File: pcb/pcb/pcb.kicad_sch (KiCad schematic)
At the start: 27 parts, among them J1 Conn_01x28_Socket, J2 Conn_01x28_Socket, J3 Conn_01x03_Socket, J4 Conn_01x04_Socket, J5 MAX17048, J6 LSM6DS3TR-C, J7 SSD1306, SW1 SW_SPST, U1 TPS61022

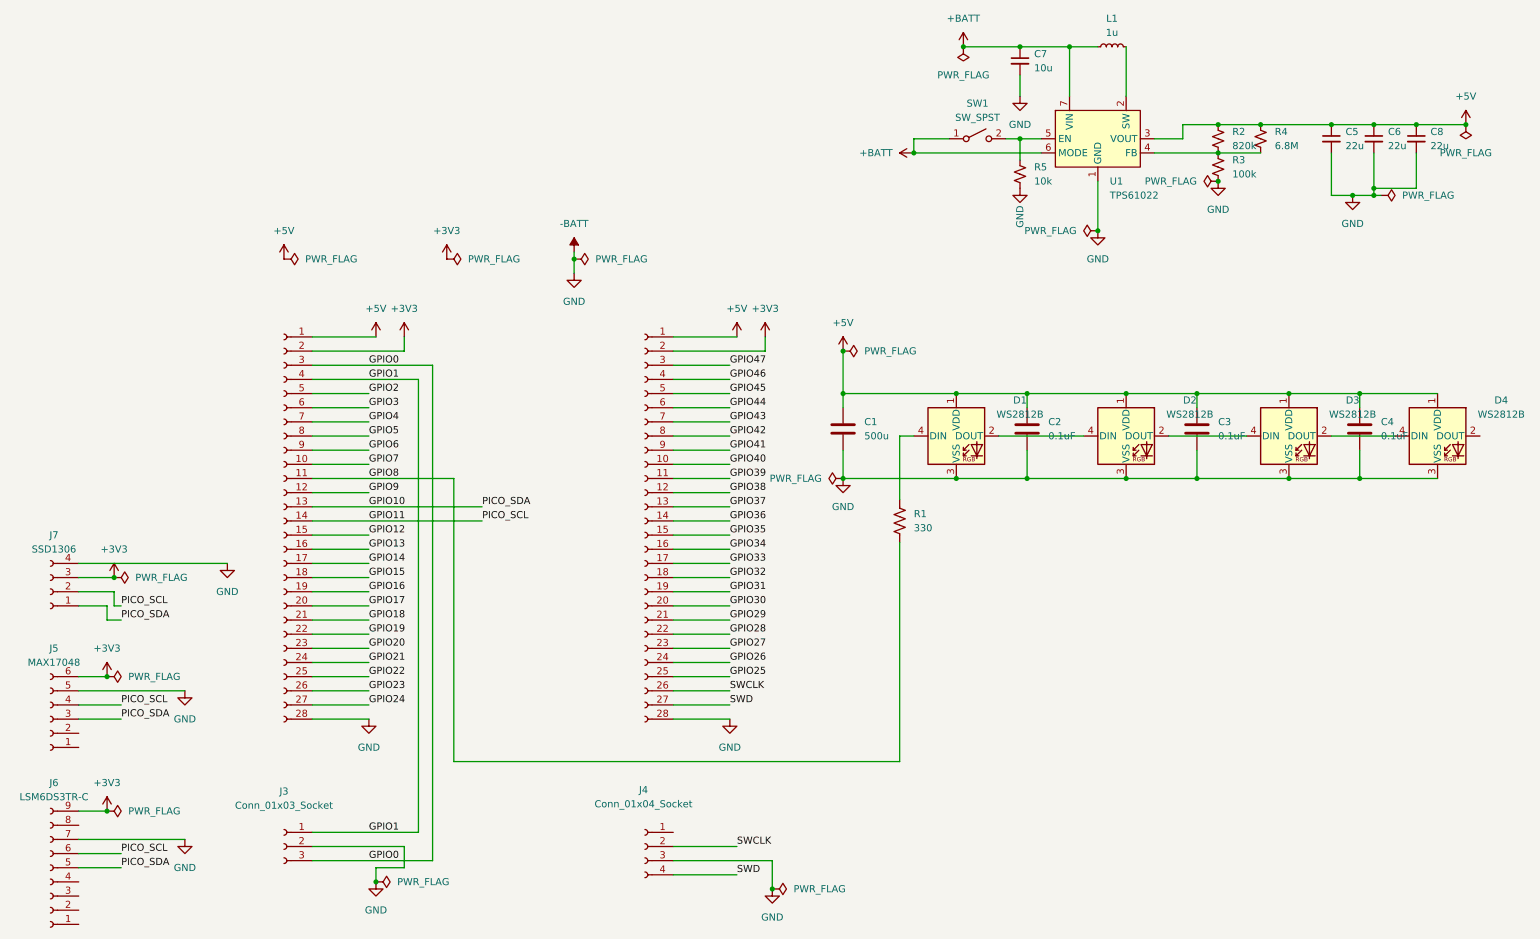
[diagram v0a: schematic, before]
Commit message: make ERC happier
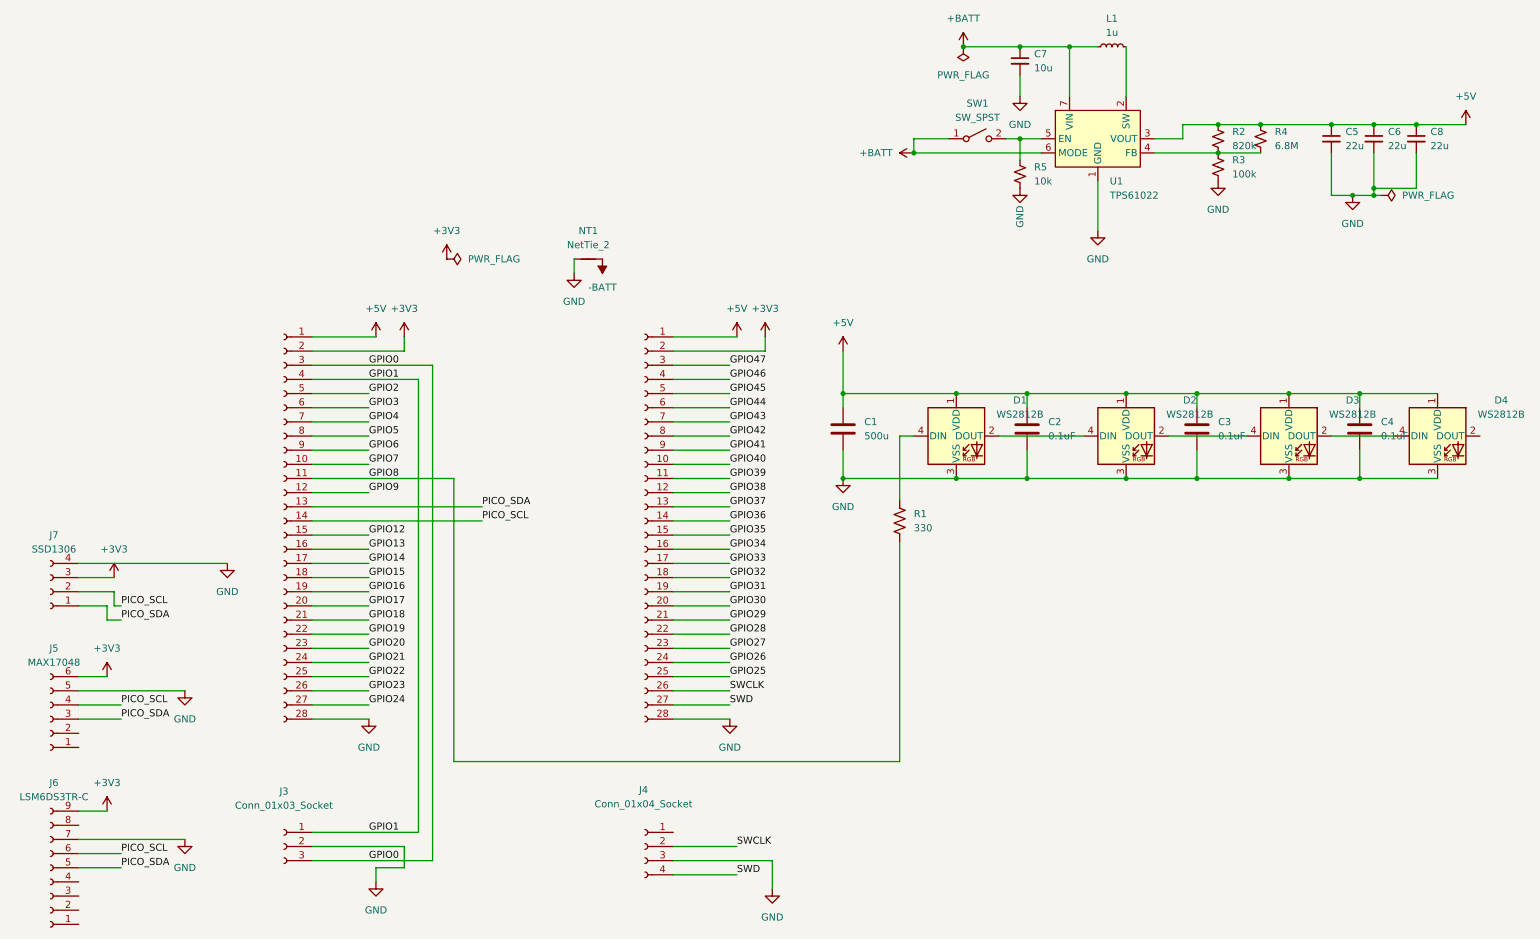
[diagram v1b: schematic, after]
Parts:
- added NT1: NetTie_2, symbol Device:NetTie_2
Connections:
- net -BATT: now also NT1.2; no longer C1.2, C2.2, C3.2, C4.2, C5.2, C6.2, C7.2, C8.2, D1.3 (VSS), D2.3 (VSS), D3.3 (VSS), D4.3 (VSS), J1.28 (Pin_28), J2.28 (Pin_28), J3.2 (Pin_2), J4.3 (Pin_3), J5.5 (Pin_5), J6.7 (Pin_7), J7.4 (Pin_4), R3.2, R5.2, U1.1 (GND)
- net GPIO10 renamed PICO_SDA
- net GPIO11 renamed PICO_SCL
- new net GND: C1.2, C2.2, C3.2, C4.2, C5.2, C6.2, C7.2, C8.2, D1.3 (VSS), D2.3 (VSS), D3.3 (VSS), D4.3 (VSS), J1.28 (Pin_28), J2.28 (Pin_28), J3.2 (Pin_2), J4.3 (Pin_3), J5.5 (Pin_5), J6.7 (Pin_7), J7.4 (Pin_4), NT1.1, R3.2, R5.2, U1.1 (GND)
